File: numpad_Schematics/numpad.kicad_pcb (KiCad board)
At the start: 11 copper layers, 75.4 x 104 mm, 44 parts, among them J1 Encoder input, J2 power module input, J3 Display, U1 ESP32-DEVKIT-V1 Matrix Handler, U2 BOB-12009

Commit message: case and pcb design
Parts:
- removed U1: ESP32-DEVKIT-V1 Matrix Handler, tigmitNIGHTLY:ESP32 Vroom Devkit V1 no holes
- added C1: 10uF, Capacitor_Tantalum_SMD:CP_EIA-3528-12_Kemet-T, B.Cu at (68.5, 40.2)
- added C2: 0.1uF, Capacitor_Tantalum_SMD:CP_EIA-3528-12_Kemet-T, B.Cu at (68.5, 35.9)
- added C3: tbd, Capacitor_Tantalum_SMD:CP_EIA-3528-12_Kemet-T, B.Cu at (68.5, 31.5)
- added J4: UART Download, Connector_PinHeader_2.54mm:PinHeader_1x03_P2.54mm_Horizontal, F.Cu at (54.5, 32.8)
- added R6: 10K, tigmitNIGHTLY:R_Axial_DIN0204_L3.6mm_D1.6mm_P7.62mm_Horizontal, F.Cu at (90.1, 35.5)
- added SW18: SW_Push, tigmitNIGHTLY:tigmit pushbutton, B.Cu at (85.0, 61.9)
- added U3: ESP32-WROOM-32, tigmitNIGHTLY:ESP32-WROOM-32 tigmit, F.Cu at (77.4, 35.7)
- D1, D10, D11, D12, D13, D14, D15, D16, D17, D2, D3, D4, D5, D6, D7, D8, D9: footprint TIGMIT_KEYBOARD_FOOTPRINTS:Diode_SOD-123 -> tigmitNIGHTLY:Diode_SOD-123
- J1: footprint TIGMIT_KEYBOARD_FOOTPRINTS:PinHeader_1x05_P2.54mm_Vertical -> tigmitNIGHTLY:PinHeader_1x05_P2.54mm_Vertical; moved to F.Cu
- J2: value power module input -> pwr input; footprint TIGMIT_KEYBOARD_FOOTPRINTS:PinHeader_1x04_P2.54mm_Vertical -> tigmitNIGHTLY:PinHeader_1x05_P2.54mm_Vertical
- J3: footprint TIGMIT_KEYBOARD_FOOTPRINTS:PinHeader_1x04_P2.54mm_Vertical -> tigmitNIGHTLY:PinHeader_1x04_P2.54mm_Vertical
- R1, R2, R3, R4, R5: footprint TIGMIT_KEYBOARD_FOOTPRINTS:R_Axial_DIN0204_L3.6mm_D1.6mm_P7.62mm_Horizontal -> tigmitNIGHTLY:R_Axial_DIN0204_L3.6mm_D1.6mm_P7.62mm_Horizontal
- SW1, SW10, SW11, SW12, SW13, SW14, SW15, SW16, SW17, SW2, SW3, SW4, SW5, SW6, SW7, SW8, SW9: footprint TIGMIT_KEYBOARD_FOOTPRINTS:hotswap socket with neopixel -> tigmitNIGHTLY:hotswap socket with neopixel
- U2: footprint TIGMIT_KEYBOARD_FOOTPRINTS:CONV_BOB-12009 -> tigmitNIGHTLY:CONV_BOB-12009
- moved D8 58.0 mm to (66.7, 91.1), turned to -55 degrees
- moved SW8 57.9 mm to (59.3, 92.0)
- moved SW15 48.6 mm to (68.8, 130.1)
- moved D15 48.3 mm to (76.6, 129.4), turned to -55 degrees
- moved J3 39.9 mm to (64.7, 82.7)
- moved J1 36.6 mm to (58.2, 38.9), turned to 180 degrees
- moved U2 33.4 mm to (116.7, 68.2), turned to -90 degrees
- moved D16 28.9 mm to (105.2, 129.3)
- moved SW16 28.6 mm to (97.4, 130.1)
- moved SW11 21.3 mm to (116.4, 82.5)
- moved SW17 21.3 mm to (116.4, 120.6)
- moved D11 21.1 mm to (123.6, 81.2), turned to -90 degrees
- moved D17 20.9 mm to (123.6, 119.7), turned to -90 degrees
- moved D10 19.1 mm to (104.9, 90.9)
- moved D9 19.1 mm to (85.8, 90.9)
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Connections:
- net NEOPIXEL5VData renamed NEOPIXEL5VData_KEYS
- J2 pad 1: batt_chargesense -> GND
- J2 pad 2: batt_voltage_Pin -> LV
- J2 pad 3: GND -> HV
- J2 pad 4: HV -> batt_chargesense
- J3 pad 1: SDA -> GND
- J3 pad 2: SCL -> LV
- J3 pad 3: LV -> SCL
- J3 pad 4: GND -> SDA
- R1 pad 1: Col2 -> Row0
- SW1 pad 1: Col2 -> Row0
- SW2 pad 1: Col2 -> Row0
- SW3 pad 1: Col2 -> Row0
- SW4 pad 1: Col2 -> Row0
- U2 pad LV1: NEOPIXEL_CONTROLL -> NEOPIXEL_CONTROLL_KEYS
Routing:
- net HV: track 0.00 -> 385.7 mm, vias 0 -> 14
- net LV: track 0.00 -> 201.0 mm, vias 0 -> 5
- net Row4: track 0.00 -> 151.3 mm, vias 0 -> 5
- net Row2: track 0.00 -> 128.6 mm, vias 0 -> 6
- net Row3: track 0.00 -> 123.1 mm, vias 0 -> 5
- net Col3: track 0.00 -> 117.3 mm, vias 0 -> 1
- net Col2: track 0.00 -> 109.5 mm, vias 0 -> 1
- net Col0: track 0.00 -> 106.5 mm, vias 0 -> 1
- net Net-(SW11-DO): track 0.00 -> 103.0 mm, vias 0 -> 2
- net Row0: track 0.00 -> 94.7 mm, vias 0 -> 5
- net Net-(SW4-DO): track 0.00 -> 94.3 mm, vias 0 -> 2
- net batt_chargesense: track 0.00 -> 94.1 mm, vias 0 -> 3
- net Row1: track 0.00 -> 85.3 mm, vias 0 -> 5
- net NEOPIXEL5VData_KEYS: track 0.00 -> 77.3 mm, vias 0 -> 2
- net batt_voltage_Pin: track 0.00 -> 75.9 mm, vias 0 -> 1
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- added copper zone on B.Cu, net GND
- added copper zone on F.Cu, net GND
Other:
- board size 75.4 x 104 mm -> 74.6 x 113.5 mm
- board text added: "GND |3.3V | 5V | bSense | vBatt"

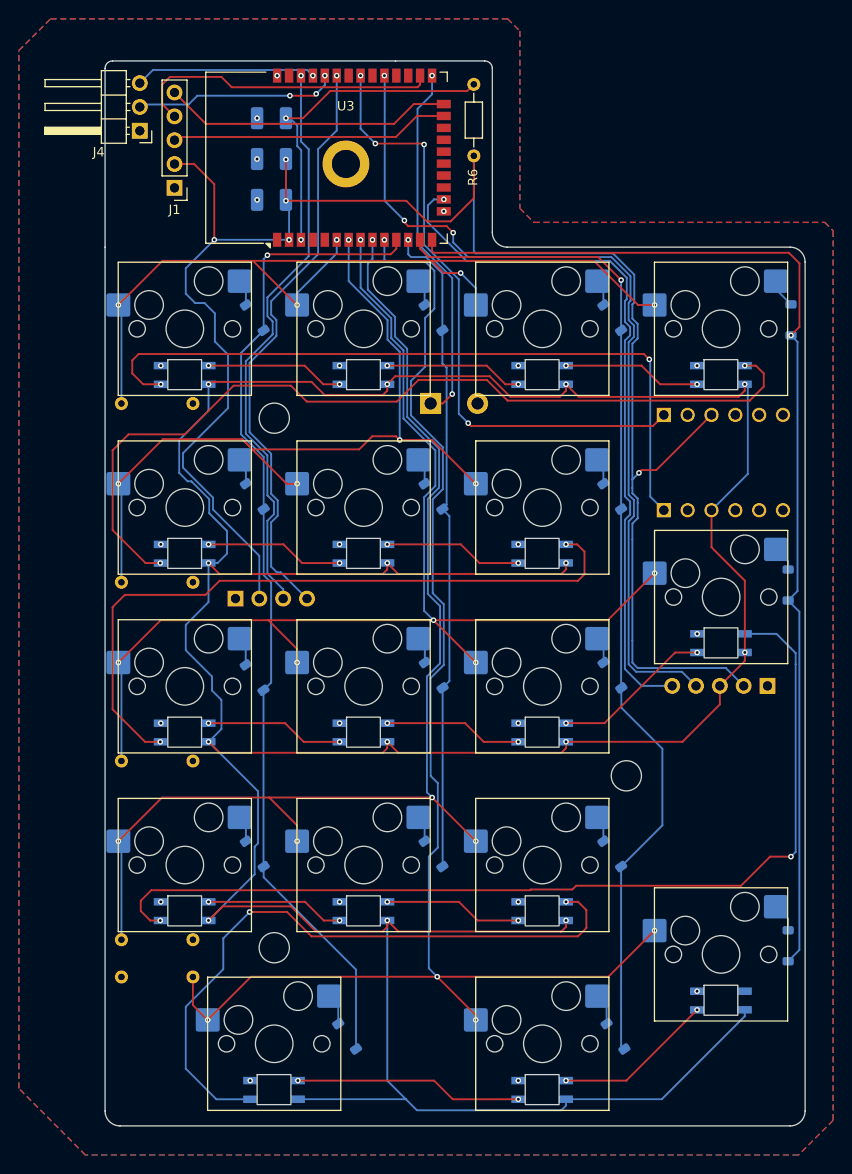
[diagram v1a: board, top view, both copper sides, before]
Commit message: case design and some software changes
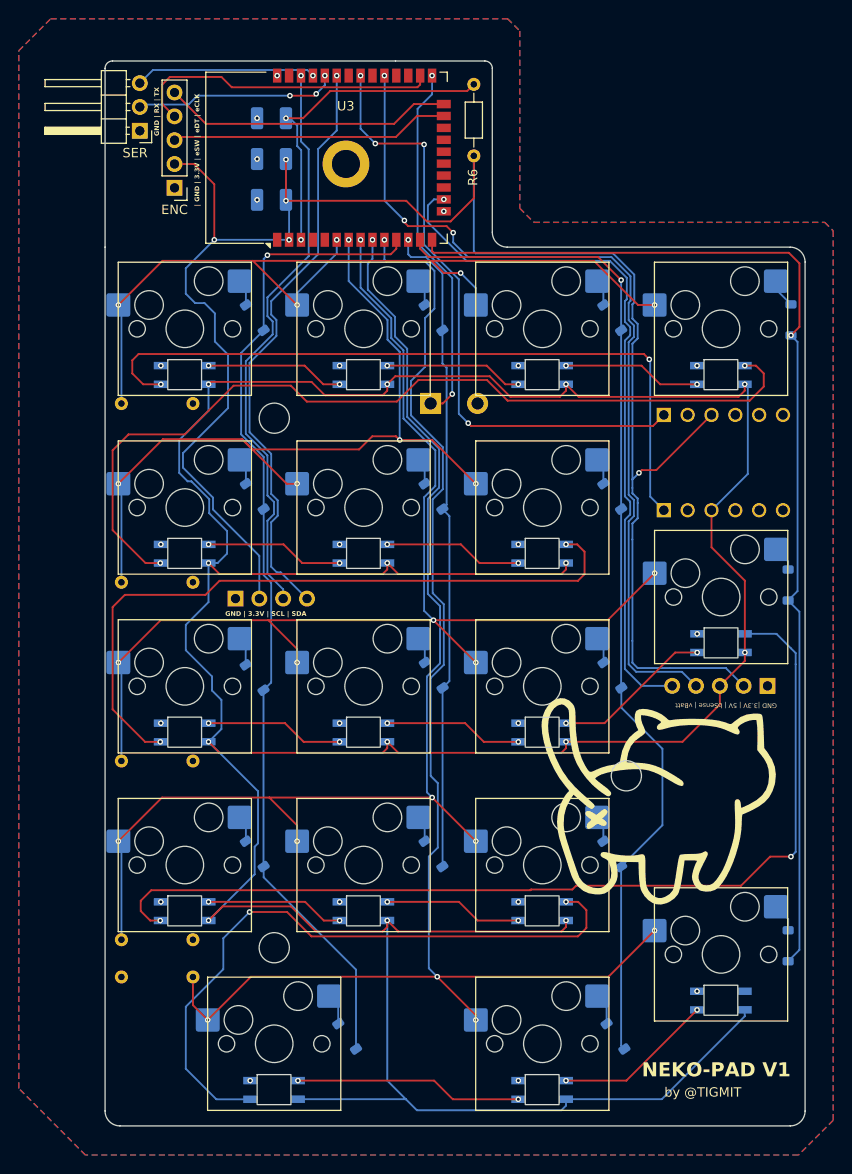
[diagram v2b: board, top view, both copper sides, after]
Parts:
- added REF**: LOGO, tigmitNIGHTLY:NekoPowerModImmage, F.Cu at (109.8, 104.3)
- LVL SHIFTER: renamed from U2
- renumbered J3 to DSPL, J1 to ENC, J2 to PWR, J4 to SER
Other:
- board text added: "GND | 3.3V | SCL | SDA"
- board text added: "GND | RX | TX"
- board text added: "NEKO-PAD V1"
- board text added: "by @TIGMIT"
- board text added: "| GND | 3.3V | eSW | eDT | eCLK"
